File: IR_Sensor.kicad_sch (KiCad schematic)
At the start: 30 parts, among them J8 Conn_01x03_Female, Q1 AO3401, Q3 NJL7302L-F3, Q31 Q_NPN_BEC, U12 AE-BME280, U17 OSRB38C9AA, U26 CM1293A-04SO

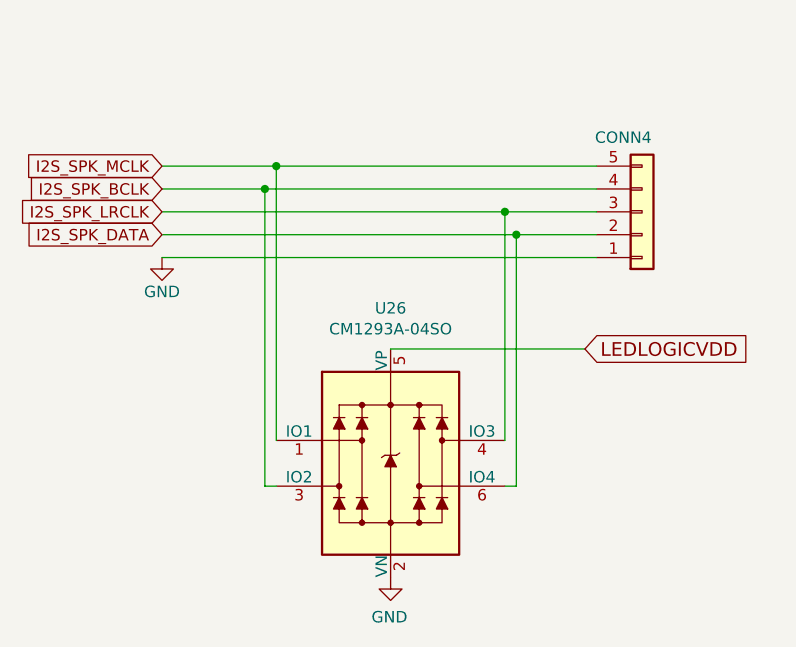
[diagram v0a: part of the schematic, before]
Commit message: Button component change and removed some ESD diodes
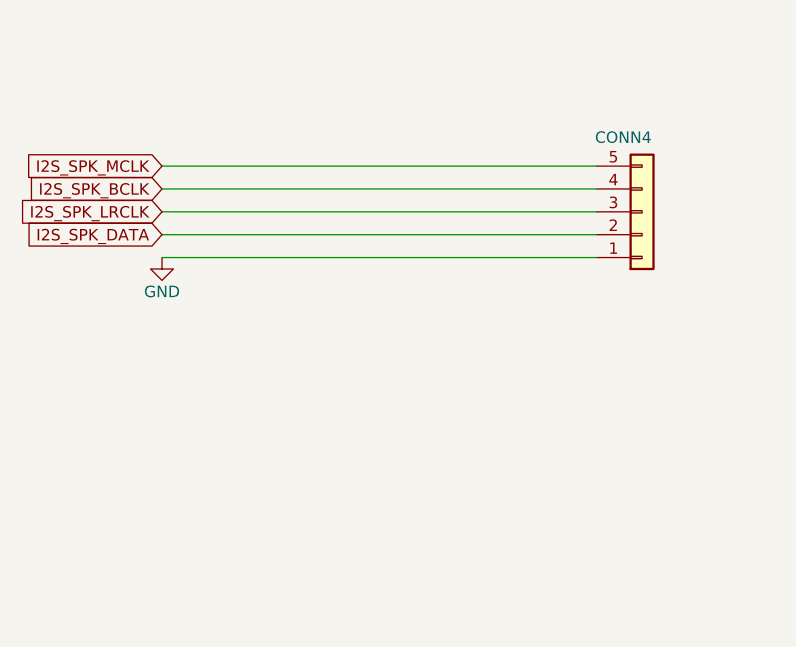
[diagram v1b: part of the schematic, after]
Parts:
- removed U26: CM1293A-04SO, components:SOT-23-6_Handsoldering_mod, symbol dotmatrix_64x48-rescue:SRV05-4-ESD_Protection
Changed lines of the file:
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@@
   (junction (at 187.96 41.91))
   (junction (at 196.85 41.91))
-  (junction (at 224.79 113.03))
-  (junction (at 226.06 110.49))
-  (junction (at 251.46 115.57))
-  (junction (at 252.73 118.11))
   (no_connect (at 199.39 38.1))
   (wire (pts (xy 25.4 39.37) (xy 34.29 39.37))
@@
     (stroke (width 0) (type solid) (color 0 0 0 0))
   )
-  (wire (pts (xy 213.36 113.03) (xy 224.79 113.03))
-    (stroke (width 0) (type solid) (color 0 0 0 0))
-  )
-  (wire (pts (xy 213.36 118.11) (xy 252.73 118.11))
-    (stroke (width 0) (type solid) (color 0 0 0 0))
-  )
-  (wire (pts (xy 224.79 113.03) (xy 261.62 113.03))
-    (stroke (width 0) (type solid) (color 0 0 0 0))
-  )
-  (wire (pts (xy 224.79 146.05) (xy 224.79 113.03))
-    (stroke (width 0) (type solid) (color 0 0 0 0))
-  )
-  (wire (pts (xy 226.06 110.49) (xy 213.36 110.49))
-    (stroke (width 0) (type solid) (color 0 0 0 0))
-  )
-  (wire (pts (xy 226.06 140.97) (xy 226.06 110.49))
-    (stroke (width 0) (type solid) (color 0 0 0 0))
-  )
-  (wire (pts (xy 226.06 146.05) (xy 224.79 146.05))
-    (stroke (width 0) (type solid) (color 0 0 0 0))
-  )
-  (wire (pts (xy 238.76 130.81) (xy 260.35 130.81))
-    (stroke (width 0) (type solid) (color 0 0 0 0))
-  )
-  (wire (pts (xy 251.46 115.57) (xy 213.36 115.57))
-    (stroke (width 0) (type solid) (color 0 0 0 0))
-  )
-  (wire (pts (xy 251.46 140.97) (xy 251.46 115.57))
-    (stroke (width 0) (type solid) (color 0 0 0 0))
-  )
-  (wire (pts (xy 251.46 146.05) (xy 252.73 146.05))
-    (stroke (width 0) (type solid) (color 0 0 0 0))
-  )
-  (wire (pts (xy 252.73 118.11) (xy 261.62 118.11))
-    (stroke (width 0) (type solid) (color 0 0 0 0))
-  )
-  (wire (pts (xy 252.73 146.05) (xy 252.73 118.11))
-    (stroke (width 0) (type solid) (color 0 0 0 0))
-  )
-  (wire (pts (xy 261.62 110.49) (xy 226.06 110.49))
-    (stroke (width 0) (type solid) (color 0 0 0 0))
-  )
-  (wire (pts (xy 261.62 115.57) (xy 251.46 115.57))
+  (wire (pts (xy 213.36 110.49) (xy 261.62 110.49))
+    (stroke (width 0) (type solid) (color 0 0 0 0))
+  )
+  (wire (pts (xy 213.36 113.03) (xy 261.62 113.03))
+    (stroke (width 0) (type solid) (color 0 0 0 0))
+  )
+  (wire (pts (xy 213.36 115.57) (xy 261.62 115.57))
+    (stroke (width 0) (type solid) (color 0 0 0 0))
+  )
+  (wire (pts (xy 213.36 118.11) (xy 261.62 118.11))
     (stroke (width 0) (type solid) (color 0 0 0 0))
   )
@@
   (global_label "I2S_SPK_DATA" (shape input) (at 213.36 118.11 180)
     (effects (font (size 1.27 1.27)) (justify right))
-  )
-  (global_label "LEDLOGICVDD" (shape input) (at 260.35 130.81 0)
-    (effects (font (size 1.524 1.524)) (justify left))
   )
   (symbol (lib_id "dotmatrix_64x48-rescue:GND-power") (at 46.99 45.72 0) (unit 1)
@@
     (property "Datasheet" "" (id 3) (at 213.36 120.65 0))
   )
-  (symbol (lib_id "dotmatrix_64x48-rescue:GND-power") (at 238.76 156.21 0) (mirror y)
-    (in_bom yes) (on_board yes)
-    (property "Reference" "#PWR0155" (id 0) (at 238.76 162.56 0)
-      (effects (font (size 1.27 1.27)) hide)
-    )
-    (property "Value" "GND" (id 1) (at 238.633 160.6042 0))
-    (property "Footprint" "" (id 2) (at 238.76 156.21 0))
-    (property "Datasheet" "" (id 3) (at 238.76 156.21 0))
-  )
   (symbol (lib_id "dotmatrix_64x48-rescue:R-device") (at 34.29 24.13 0) (mirror y) (unit 1)
     (in_bom yes) (on_board yes)
@@
     (property "Datasheet" "" (id 3) (at 50.8 40.64 0))
   )
-  (symbol (lib_id "dotmatrix_64x48-rescue:C-device") (at 59.69 39.37 0)
+  (symbol (lib_id "dotmatrix_64x48-rescue:C-device") (at 59.69 39.37 0) (unit 1)
     (in_bom yes) (on_board yes)
     (property "Reference" "C1" (id 0) (at 63.5 39.37 0)
@@
     (property "Datasheet" "" (id 3) (at 53.34 83.82 0))
   )
-  (symbol (lib_id "dotmatrix_64x48-rescue:Q_PMOS_GSD-device") (at 86.36 72.39 270) (mirror x)
+  (symbol (lib_id "dotmatrix_64x48-rescue:Q_PMOS_GSD-device") (at 86.36 72.39 270) (mirror x) (unit 1)
     (in_bom yes) (on_board yes)
     (property "Reference" "Q1" (id 0) (at 85.1916 67.5386 0)
@@
     )
   )
-  (symbol (lib_id "dotmatrix_64x48-rescue:SRV05-4-ESD_Protection") (at 238.76 143.51 0)
-    (in_bom yes) (on_board yes)
-    (property "Reference" "U26" (id 0) (at 238.76 126.2888 0))
-    (property "Value" "CM1293A-04SO" (id 1) (at 238.76 128.6002 0))
-    (property "Footprint" "components:SOT-23-6_Handsoldering_mod" (id 2) (at 238.76 143.51 0)
-      (effects (font (size 1.27 1.27)) hide)
-    )
-    (property "Datasheet" "http://www.onsemi.com/pub/Collateral/SRV05-4-D.PDF" (id 3) (at 238.76 143.51 0)
-      (effects (font (size 1.27 1.27)) hide)
-    )
-  )

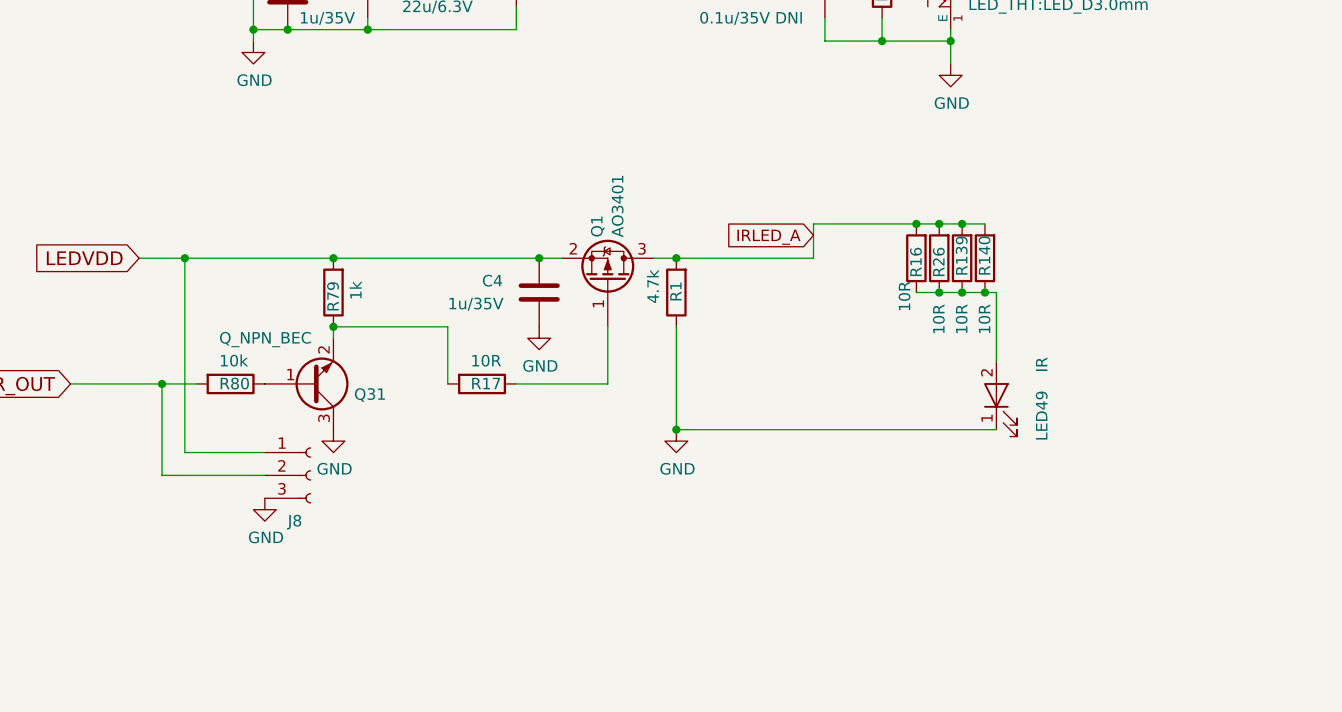
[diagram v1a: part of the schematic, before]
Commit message: Added C80 / removed orphan GND in the schematics
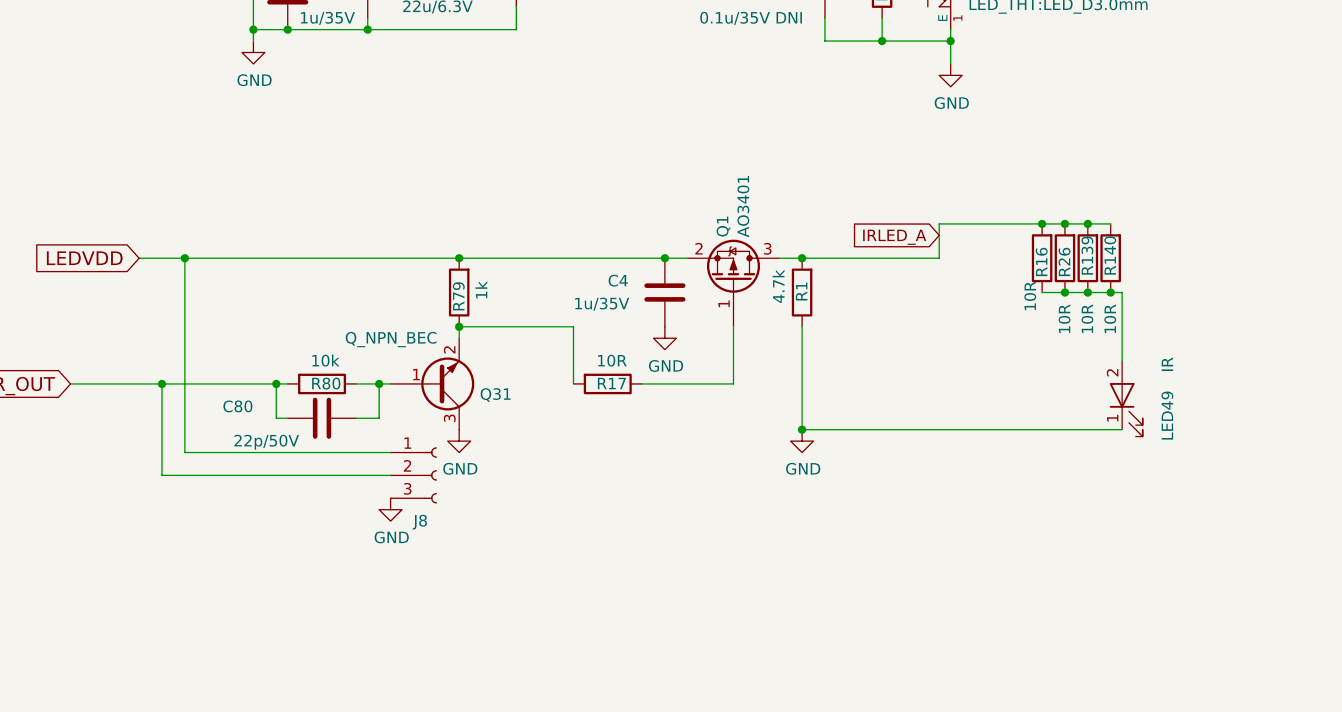
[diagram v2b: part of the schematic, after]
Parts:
- added C80: 22p/50V, Capacitor_SMD:C_0603_1608Metric_Pad1.05x0.95mm_HandSolder, symbol dotmatrix_64x48-rescue:C-device
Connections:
- net IR_OUT: now also C80.1
- net at Q31.1 (B), R80.1: now also C80.2
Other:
- moved on the sheet: C4, J8, LED49, Q1, Q31, R1, R139, R140, R16, R17, R26, R79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

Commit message: Swapped Q31 E/C / DRC clear
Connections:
- net GND: now also Q31.2 (E); no longer Q31.3 (C)
- net at R17.2, R79.1: now also Q31.3 (C); no longer Q31.2 (E)
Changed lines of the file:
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@@
     (property "Datasheet" "" (id 3) (at 266.7 115.57 0))
   )
-  (symbol (lib_id "dotmatrix_64x48-rescue:Q_NPN_BEC-device") (at 67.31 83.82 0) (mirror x) (unit 1)
+  (symbol (lib_id "dotmatrix_64x48-rescue:Q_NPN_BEC-device") (at 67.31 83.82 0) (unit 1)
     (in_bom yes) (on_board yes)
-    (property "Reference" "Q31" (id 0) (at 72.136 84.9884 0)
+    (property "Reference" "Q31" (id 0) (at 72.136 82.6516 0)
       (effects (font (size 1.27 1.27)) (justify left))
     )
-    (property "Value" "Q_NPN_BEC" (id 1) (at 57.15 78.74 0)
+    (property "Value" "Q_NPN_BEC" (id 1) (at 57.15 88.9 0)
       (effects (font (size 1.27 1.27)) (justify left))
     )
-    (property "Footprint" "Package_TO_SOT_SMD:SOT-23_Handsoldering" (id 2) (at 72.1614 81.5086 0)
+    (property "Footprint" "Package_TO_SOT_SMD:SOT-23_Handsoldering" (id 2) (at 72.1614 86.1314 0)
       (effects (font (size 1.27 1.27)) (justify left) hide)
     )
